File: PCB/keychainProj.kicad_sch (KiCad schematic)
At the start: 34 parts, among them J1 Conn_01x04_Pin, J2 USB_C_Receptacle_PowerOnly_6P, SW1 SW_SPDT_MSM, U1 AMS1117CD-3.3, U2 LIS3DH, U4 CH32V003FxPx

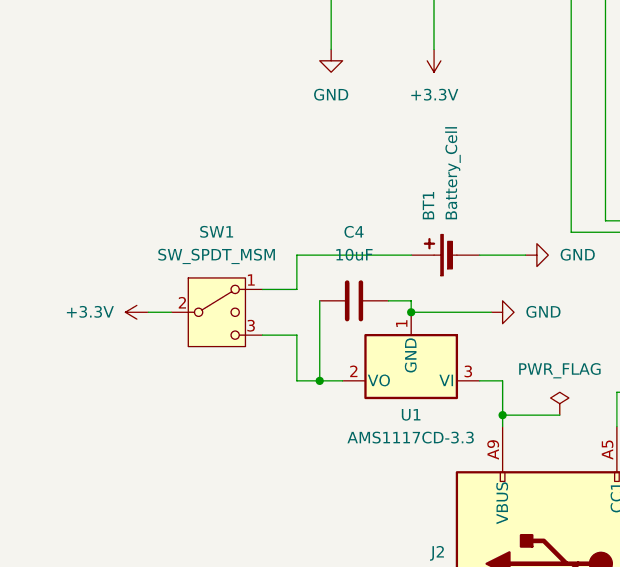
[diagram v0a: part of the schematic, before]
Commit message: Simplified PCB and made for in depth bom files
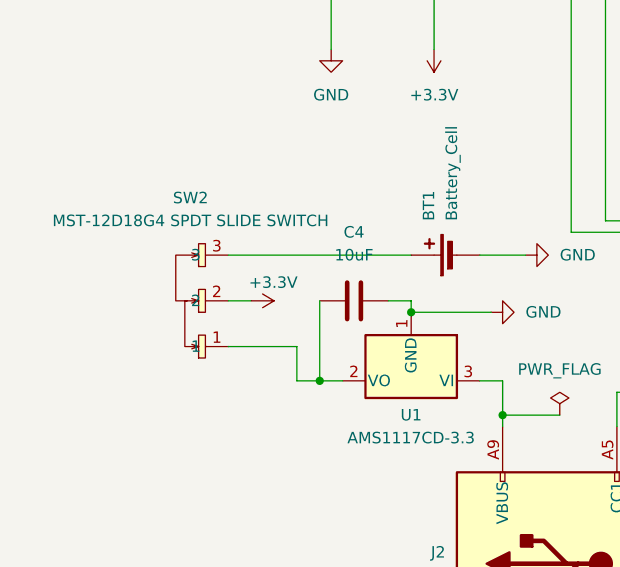
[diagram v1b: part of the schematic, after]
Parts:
- removed SW1: SW_SPDT_MSM, Button_Switch_THT:SW_Slide_SPDT_Straight_CK_OS102011MS2Q, symbol Switch:SW_SPDT_MSM
- added SW2: MST-12D18G4 SPDT SLIDE SWITCH, Newsymbols:SW-SMD_MST-12D18G4-SPDT-SLIDE-SWITCH, symbol MST-12D18G4_SPDT_SLIDE_SWITCH:MST-12D18G4SPDTSLIDESWITCH
- R5, R6: value 47 -> 0
- U2: footprint Package_LGA:LGA-16_3x3mm_P0.5mm_LayoutBorder3x5y -> ModuleLibrary:LIS3DH_Aliexpress_Module
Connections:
- net +3.3V: now also SW2.2
- net at BT1.1 (+): now also SW2.3
- net at C4.1, U1.2 (VO): now also SW2.1
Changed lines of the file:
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@@
 	(wire
 		(pts
-			(xy 36.83 162.56) (xy 33.02 162.56)
-		)
-		(stroke
-			(width 0)
-			(type default)
-		)
-	)
-	(wire
-		(pts
 			(xy 196.85 82.55) (xy 196.85 87.63)
 		)
@@
 	(wire
 		(pts
+			(xy 29.21 158.75) (xy 31.75 158.75)
+		)
+		(stroke
+			(width 0)
+			(type default)
+		)
+	)
+	(wire
+		(pts
 			(xy 173.99 68.58) (xy 185.42 68.58)
 		)
@@
 	(wire
 		(pts
-			(xy 36.83 157.48) (xy 33.02 157.48)
-		)
-		(stroke
-			(width 0)
-			(type default)
-		)
-	)
-	(wire
-		(pts
 			(xy 71.12 123.19) (xy 83.82 123.19)
 		)
@@
 	(wire
 		(pts
-			(xy 49.53 153.67) (xy 36.83 153.67)
-		)
-		(stroke
-			(width 0)
-			(type default)
-		)
-	)
-	(wire
-		(pts
 			(xy 125.73 143.51) (xy 128.27 143.51)
 		)
@@
 	(wire
 		(pts
+			(xy 29.21 163.83) (xy 36.83 163.83)
+		)
+		(stroke
+			(width 0)
+			(type default)
+		)
+	)
+	(wire
+		(pts
 			(xy 194.31 101.6) (xy 194.31 106.68)
 		)
@@
 	(wire
 		(pts
-			(xy 36.83 167.64) (xy 36.83 162.56)
+			(xy 36.83 167.64) (xy 36.83 163.83)
 		)
 		(stroke
@@
 	(wire
 		(pts
-			(xy 20.32 160.02) (xy 22.86 160.02)
-		)
-		(stroke
-			(width 0)
-			(type default)
-		)
-	)
-	(wire
-		(pts
 			(xy 57.15 167.64) (xy 59.69 167.64)
 		)
@@
 	(wire
 		(pts
-			(xy 36.83 153.67) (xy 36.83 157.48)
+			(xy 29.21 153.67) (xy 49.53 153.67)
 		)
 		(stroke
@@
 			)
 		)
-		(property "Value" "47"
+		(property "Value" "0"
 			(at 129.5399 71.12 0)
 			(hide yes)
@@
 	(symbol
 		(lib_id "power:+3.3V")
-		(at 20.32 160.02 90)
+		(at 31.75 158.75 270)
 		(unit 1)
 		(body_style 1)
@@
 		(in_pos_files yes)
 		(dnp no)
-		(fields_autoplaced yes)
 		(property "Reference" "#PWR02"
-			(at 24.13 160.02 0)
+			(at 27.94 158.75 0)
 			(hide yes)
 			(show_name no)
@@
 		)
 		(property "Value" "+3.3V"
-			(at 16.51 160.0199 90)
+			(at 31.496 156.718 90)
 			(show_name no)
 			(do_not_autoplace no)
@@
 		)
 		(property "Footprint" ""
-			(at 20.32 160.02 0)
+			(at 31.75 158.75 0)
 			(hide yes)
 			(show_name no)
@@
 		)
 		(property "Datasheet" ""
-			(at 20.32 160.02 0)
+			(at 31.75 158.75 0)
 			(hide yes)
 			(show_name no)
@@
 		)
 		(property "Description" "Power symbol creates a global label with name \"+3.3V\""
-			(at 20.32 160.02 0)
+			(at 31.75 158.75 0)
 			(hide yes)
 			(show_name no)
@@
 	)
 	(symbol
+		(lib_id "MST-12D18G4_SPDT_SLIDE_SWITCH:MST-12D18G4SPDTSLIDESWITCH")
+		(at 26.67 160.02 90)
+		(unit 1)
+		(body_style 1)
+		(exclude_from_sim no)
+		(in_bom yes)
+		(on_board yes)
+		(in_pos_files yes)
+		(dnp no)
+		(fields_autoplaced yes)
+		(property "Reference" "SW2"
+			(at 25.02 147.32 90)
+			(show_name no)
+			(do_not_autoplace no)
+			(effects
+				(font
+					(size 1.27 1.27)
+				)
+			)
+		)
+		(property "Value" "MST-12D18G4 SPDT SLIDE SWITCH"
+			(at 25.02 149.86 90)
+			(show_name no)
+			(do_not_autoplace no)
+			(effects
+				(font
+					(size 1.27 1.27)
+				)
+			)
+		)
+		(property "Footprint" "Newsymbols:SW-SMD_MST-12D18G4-SPDT-SLIDE-SWITCH"
+			(at 36.83 160.02 0)
+			(hide yes)
+			(show_name no)
+			(do_not_autoplace no)
+			(effects
+				(font
+					(size 1.27 1.27)
+				)
+			)
+		)
+		(property "Datasheet" "https://www.lcsc.com/datasheet/C49023767.pdf"
+			(at 39.37 160.02 0)
+			(hide yes)
+			(show_name no)
+			(do_not_autoplace no)
+			(effects
+				(font
+					(size 1.27 1.27)
+				)
+			)
+		)
+		(property "Description" ""
+			(at 26.67 160.02 0)
+			(hide yes)
+			(show_name no)
+			(do_not_autoplace no)
+			(effects
+				(font
+					(size 1.27 1.27)
+				)
+			)
+		)
+		(property "Manufacturer" "SHOU HAN(首韩)"
+			(at 41.91 160.02 0)
+			(hide yes)
+			(show_name no)
+			(do_not_autoplace no)
+			(effects
+				(font
+					(size 1.27 1.27)
+				)
+			)
+		)
+		(property "MPN" "MST-12D18G4 SPDT Slide Switch"
+			(at 44.45 160.02 0)
+			(hide yes)
+			(show_name no)
+			(do_not_autoplace no)
+			(effects
+				(font
+					(size 1.27 1.27)
+				)
+			)
+		)
+		(property "LCSC Part" "C49023767"
+			(at 46.99 160.02 0)
+			(hide yes)
+			(show_name no)
+			(do_not_autoplace no)
+			(effects
+				(font
+					(size 1.27 1.27)
+				)
+			)
+		)
+		(pin "3"
+		)
+		(pin "1"
+		)
+		(pin "2"
+		)
+		(instances
+			(project "keychainProj"
+				(path "/e6e2aaf7-f887-43da-a319-215922018b95"
+					(reference "SW2")
+					(unit 1)
+				)
+			)
+		)
+	)
+	(symbol
 		(lib_id "power:GND")
 		(at 147.32 115.57 270)
@@
 			)
 		)
-		(property "Value" "47"
+		(property "Value" "0"
 			(at 129.5399 76.2 0)
 			(hide yes)
@@
 		(in_bom no)
 		(on_board yes)
-		(in_pos_files yes)
+		(in_pos_files no)
 		(dnp no)
 		(fields_autoplaced yes)
@@
 			)
 		)
-		(property "Footprint" "Package_LGA:LGA-16_3x3mm_P0.5mm_LayoutBorder3x5y"
+		(property "Footprint" "ModuleLibrary:LIS3DH_Aliexpress_Module"
 			(at 99.06 144.78 0)
 			(hide yes)
@@
 					(unit 1)
 				)
-			)
-		)
-	)
-	(symbol
-		(lib_id "Switch:SW_SPDT_MSM")
-		(at 27.94 160.02 0)
-		(unit 1)
-		(body_style 1)
-		(exclude_from_sim no)
-		(in_bom yes)
-		(on_board yes)
-		(in_pos_files yes)
-		(dnp no)
-		(fields_autoplaced yes)
-		(property "Reference" "SW1"
-			(at 27.94 151.13 0)
-			(show_name no)
-			(do_not_autoplace no)
-			(effects
-				(font
-					(size 1.27 1.27)
-				)
-			)
-		)
-		(property "Value" "SW_SPDT_MSM"
-			(at 27.94 153.67 0)
-			(show_name no)
-			(do_not_autoplace no)
-			(effects
-				(font
-					(size 1.27 1.27)
-				)
-			)
-		)
-		(property "Footprint" "Button_Switch_THT:SW_Slide_SPDT_Straight_CK_OS102011MS2Q"
-			(at 13.97 148.59 0)
-			(hide yes)
-			(show_name no)
-			(do_not_autoplace no)
-			(effects
-				(font
-					(size 1.27 1.27)
-				)
-			)
-		)
-		(property "Datasheet" ""
-			(at 27.94 167.64 0)
-			(hide yes)
-			(show_name no)
-			(do_not_autoplace no)
-			(effects
-				(font
-					(size 1.27 1.27)
-				)
-			)
-		)
-		(property "Description" "Switch, single pole double throw, center OFF position"
-			(at 27.94 160.02 0)
-			(hide yes)
-			(show_name no)
-			(do_not_autoplace no)
-			(effects
-				(font
-					(size 1.27 1.27)
-				)
-			)
-		)
-		(pin "3"
-		)
-		(pin "1"
-		)
-		(pin "2"
-		)
-		(instances
-			(project "keychainProj"
-				(path "/e6e2aaf7-f887-43da-a319-215922018b95"
-					(reference "SW1")
-					(unit 1)
-				)
